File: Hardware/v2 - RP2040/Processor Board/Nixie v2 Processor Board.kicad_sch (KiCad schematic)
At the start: 82 parts, among them J1 Conn_01x10_Socket, J2 USB_C_Receptacle_USB2.0, J3 Conn_01x03_2.54mm, J4 Conn_01x03_2.54mm, J5 AudioJack3_SwitchT, J6 Conn_01x10_Socket, J8 Conn_01x01_Pin, J9 Conn_01x10_Socket, Q1 PZTA92, Q3 MMBTA42, SW1 SW_Push, SW2 SW_Push, SW3 SW_DIP_x10, SW4 SW_Push, U1 NCH8200HV, U10 W25Q128JVP, U12 DS3231MZ, U14 VEML7700, U3 TPS62933, U7 MCP23017_ML, U8 AP22913, U9 RP2040, Y1 12MHz

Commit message: seperated the processor and nixie boards
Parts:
- removed C2: 4.7u, Capacitor_THT:CP_Radial_D8.0mm_P3.50mm, symbol Device:C_Polarized_Small_US
- removed C3, C31, C5: 100n, Capacitor_SMD:C_0603_1608Metric, symbol Device:C_Small
- removed C30: 10u, symbol Device:C_Polarized_Small_US
- removed C4: 10u, Capacitor_SMD:C_0603_1608Metric, symbol Device:C_Small
- removed C6: 82p, Capacitor_SMD:C_0603_1608Metric, symbol Device:C_Small
- removed C7: 33n, Capacitor_SMD:C_0603_1608Metric, symbol Device:C_Small
- removed C8: 47u, Capacitor_SMD:C_0603_1608Metric, symbol Device:C_Small
- removed L1: 7.8u, Inductor_SMD:L_Vishay_IHLP-5050, symbol Device:L
- removed Q1: PZTA92, Package_TO_SOT_SMD:SOT-223-3_TabPin2, symbol Transistor_BJT:PZTA92
- removed Q3: MMBTA42, Package_TO_SOT_SMD:SOT-23, symbol Transistor_BJT:MMBTA42
- removed R17: 30.9, Resistor_SMD:R_0603_1608Metric, symbol Device:R_Small_US
- removed R18, R7: 10k, Resistor_SMD:R_0603_1608Metric, symbol Device:R_Small_US
- removed R28, R29: 2.2k, Resistor_SMD:R_0603_1608Metric, symbol Device:R_Small_US
- removed R5: 100k, Resistor_SMD:R_0603_1608Metric, symbol Device:R_Small_US
- removed TP3: TestPoint, symbol Connector:TestPoint
- removed U1: NCH8200HV, symbol Nick-Nixie:NCH8200HV
- removed U14: VEML7700, symbol Nick_Sensor:VEML7700
- removed U3: TPS62933, Package_TO_SOT_SMD:SOT-583-8, symbol Regulator_Switching:TPS62933
- added C19: 1u, Capacitor_SMD:C_0402_1005Metric, symbol Device:C_Small
- added C2: 22u, Capacitor_SMD:C_0603_1608Metric, symbol Device:C_Small
- added JP1: SolderJumper_3_Open, Jumper:SolderJumper-3_P1.3mm_Open_RoundedPad1.0x1.5mm, symbol Jumper:SolderJumper_3_Open
- added R10: 2.2k, Resistor_SMD:R_0603_1608Metric, symbol Device:R_Small_US
- added R13: 10k, Resistor_SMD:R_0603_1608Metric, symbol Device:R_Small_US
- added TP10, TP6, TP7, TP8, TP9: TestPoint, TestPoint:TestPoint_Pad_D2.0mm, symbol Connector:TestPoint
- added U1: TPS82084SIL, symbol Nick_Converter:TPS82084SIL
- C1: value 100u -> 10u
- C10: renamed from C14; footprint Capacitor_SMD:C_0603_1608Metric -> Capacitor_SMD:C_0402_1005Metric
- C11: renamed from C15; footprint Capacitor_SMD:C_0603_1608Metric -> Capacitor_SMD:C_0402_1005Metric
- C12: renamed from C16; footprint Capacitor_SMD:C_0603_1608Metric -> Capacitor_SMD:C_0402_1005Metric
- C13: renamed from C17; footprint Capacitor_SMD:C_0603_1608Metric -> Capacitor_SMD:C_0402_1005Metric
- C5: renamed from C9; footprint Capacitor_SMD:C_0603_1608Metric -> Capacitor_SMD:C_0402_1005Metric
- C6: renamed from C10; footprint Capacitor_SMD:C_0603_1608Metric -> Capacitor_SMD:C_0402_1005Metric
- C7: renamed from C11; footprint Capacitor_SMD:C_0603_1608Metric -> Capacitor_SMD:C_0402_1005Metric
- C8: renamed from C12; footprint Capacitor_SMD:C_0603_1608Metric -> Capacitor_SMD:C_0402_1005Metric
- C9: renamed from C13; footprint Capacitor_SMD:C_0603_1608Metric -> Capacitor_SMD:C_0402_1005Metric
- J1: renamed from J9; footprint (none) -> Connector_PinSocket_2.54mm:PinSocket_2x05_P2.54mm_Horizontal
- J2: renamed from J1; footprint (none) -> Connector_PinSocket_2.54mm:PinSocket_2x05_P2.54mm_Horizontal
- J3: renamed from J6; footprint (none) -> Connector_PinSocket_2.54mm:PinSocket_2x05_P2.54mm_Horizontal
- J4: renamed from J8; footprint (none) -> Connector_PinHeader_2.54mm:PinHeader_1x01_P2.54mm_Vertical
- R1: value 100k -> 523k
- R2: value 10k -> 169k; footprint Resistor_SMD:R_0402_1005Metric -> Resistor_SMD:R_0603_1608Metric
- R3: value 100k -> 499k
- R9: value 10k -> 2.2k
- TP1, TP2: footprint (none) -> TestPoint:TestPoint_Pad_D2.0mm
- TP3: renamed from TP6; footprint (none) -> TestPoint:TestPoint_Pad_D2.0mm
- TP4: renamed from TP5; footprint (none) -> TestPoint:TestPoint_Pad_D2.0mm
- TP5: renamed from TP4; footprint (none) -> TestPoint:TestPoint_Pad_D2.0mm
- Y1: footprint 0_My_Footprints:Crystal_SMD_Abracon_ABM10-4Pin_2.5x2.0mm -> Crystal:Crystal_SMD_Abracon_ABM10-4Pin_2.5x2.0mm
- renumbered C18 to C14, C19 to C15, C20 to C16, C29 to C17, C21 to C18, C27 to C20, C28 to C21, C33 to C22, C35 to C23, C22 to C3, C23 to C4, J2 to J6, J3 to J7, J4 to J8, R24 to R11, R25 to R12, R27 to R14, R32 to R15, R30 to R16, R31 to R17, R19 to R4, R20 to R5, R21 to R6, R22 to R7, R23 to R8, U8 to U2, U12 to U3, U9 to U4, U10 to U5, U7 to U6
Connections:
- net Mins_Ones_A is gone; now on net Minutes_Ones_A: J2.9 (Pin_9)
- net Mins_Ones_B is gone; now on net Minutes_Ones_B: J2.7 (Pin_7)
- net Mins_Ones_C is gone; now on net Minutes_Ones_C: J2.6 (Pin_6)
- net Mins_Ones_D is gone; now on net Minutes_Ones_D: J2.8 (Pin_8)
- net Mins_Tens_A is gone; now on net Minutes_Tens_A: J2.2 (Pin_2)
- net Mins_Tens_B is gone; now on net Minutes_Tens_B: J2.4 (Pin_4)
- net Mins_Tens_C is gone; now on net Minutes_Tens_C: J2.5 (Pin_5)
- net Mins_Tens_D is gone; now on net Minutes_Tens_D: J2.3 (Pin_3)
- net +3.3V: now also J3.3 (Pin_3), R1.2, R3.2, C2.1, JP1.3 (B), U1.5 (Vout); no longer R2.2
- net +3V3: now also R9.1, R10.1, R13.1
- net Dimming: now also J3.6 (Pin_6); no longer J3.5 (Pin_5)
- net GND: now also R2.1, C19.2, C2.2, U1.5 (Vout), U1.6 (GND), U1.EP (GND); no longer R9.2
- net Hours_Tens_A: now also U4.8 (GPIO6); no longer U4.4 (GPIO2)
- net Hours_Tens_B: now also U4.11 (GPIO8); no longer J3.4 (Pin_4), U3.8 (SCL), U4.7 (GPIO5), U6.8 (SCK)
- net Hours_Tens_C: now also U4.12 (GPIO9); no longer U4.8 (GPIO6)
- net Hours_Tens_D: now also U4.9 (GPIO7); no longer U4.5 (GPIO3)
- net RTC_Interrupt: now also U4.37 (GPIO25), R13.2; no longer U4.36 (GPIO24)
- net Settings_Interrupt: now also U4.38 (GPIO26_ADC0); no longer U4.37 (GPIO25)
- net UART1_RX: now also U4.7 (GPIO5); no longer U4.12 (GPIO9)
- net UART1_TX: now also U4.6 (GPIO4); no longer U4.11 (GPIO8)
- net VBUS: now also JP1.1 (A), U1.1 (EN), U1.3 (Vin), U1.4 (Vin); no longer C3.1, U2.4 (VIN), U2.6 (VIN)
- net at U6.20 (GPA3): now also TP6.1
- net at U6.21 (GPA4): now also TP7.1
- net at U6.22 (GPA5): now also TP8.1
- net at U6.23 (GPA6): now also TP9.1
- net at U6.24 (GPA7): now also TP10.1
- net at R3.1: now also U1.2 (PG); no longer R1.2
- net at BT1.1 (+), U3.6 (VBAT): now also C19.1
- net 170V_1: no longer names the net of R1.1
- net 170V_1: now also R2.2, U1.7 (FB)
- net GPS_Presence renamed GPS_Connected
- net GPS_Connected: now also U4.36 (GPIO24); no longer U4.38 (GPIO26_ADC0)
- net I2C0_SDA renamed I2C1_SDA
- net I2C1_SDA: now also J3.4 (Pin_4), U4.4 (GPIO2), R10.2; no longer J3.3 (Pin_3), U4.6 (GPIO4)
- new net: C3.1, JP1.2 (C), U2.4 (VIN), U2.6 (VIN)
- new net I2C1_SCL: J3.5 (Pin_5), R9.2, U3.8 (SCL), U4.5 (GPIO3), U6.8 (SCK)
- no-connect marks 8 -> 3
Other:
- note added: "3mOhm"
- note added: "9mOhm"
- note added: "VBUS to 3.3V"
- note added: "Voltage select for GPS module"
- note removed: "250V or larger"
- note removed: "LIGHT SENSOR"
- note removed: "Low ESR"
- note removed: "Vin to 3.3V"
- title: Nixie Tube Clock -> Nixie Processor Board
- moved on the sheet: BT1, C10, C11, C12, C13, C14, C15, C16, C17, C18, C20, C21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

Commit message: Started board layout
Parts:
- added H1, H2, H3, H4: MountingHole_Pad, MountingHole:MountingHole_3.2mm_M3_Pad_Via, symbol Mechanical:MountingHole_Pad
- C19: footprint Capacitor_SMD:C_0402_1005Metric -> Capacitor_SMD:C_0603_1608Metric
- J5: footprint (none) -> Connector_Audio:Jack_3.5mm_CUI_SJ-3524-SMT_Horizontal
- JP1: footprint Jumper:SolderJumper-3_P1.3mm_Open_RoundedPad1.0x1.5mm -> Jumper:SolderJumper-3_P1.3mm_Open_RoundedPad1.0x1.5mm_NumberLabels
- SW3: footprint Button_Switch_SMD:SW_DIP_SPSTx10_Slide_6.7x26.96mm_W6.73mm_P2.54mm_LowProfile_JPin -> Button_Switch_THT:SW_DIP_SPSTx10_Piano_10.8x26.96mm_W7.62mm_P2.54mm
- U1: footprint (none) -> Nick_Converter_DCDC:MicroSiP 1.33mm
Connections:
- net +3.3V: now also U1.8 (Vout); no longer U1.5 (Vout)
- net GND: now also J1.5 (Pin_5), J1.6 (Pin_6), J2.5 (Pin_5), J2.6 (Pin_6), SW3.1, SW3.10, SW3.2, SW3.3, SW3.4, SW3.5, SW3.6, SW3.7, SW3.8, SW3.9, U1.9 (GND), H1.1, H2.1, H3.1, H4.1; no longer J1.1 (Pin_1), J1.10 (Pin_10), J2.1 (Pin_1), J2.10 (Pin_10), SW3.11, SW3.12, SW3.13, SW3.14, SW3.15, SW3.16, SW3.17, SW3.18, SW3.19, SW3.20, U1.EP (GND)
- net Hours_Ones_A: now also J1.3 (Pin_3), U4.11 (GPIO8); no longer J1.9 (Pin_9), U4.13 (GPIO10)
- net Hours_Ones_B: now also J1.1 (Pin_1), U4.8 (GPIO6); no longer J1.7 (Pin_7), U4.15 (GPIO12)
- net Hours_Ones_C: now also J1.2 (Pin_2), U4.9 (GPIO7); no longer J1.6 (Pin_6), U4.16 (GPIO13)
- net Hours_Ones_D: now also J1.4 (Pin_4), U4.12 (GPIO9); no longer J1.8 (Pin_8), U4.14 (GPIO11)
- net Hours_Tens_A: now also J1.10 (Pin_10), U4.16 (GPIO13); no longer J1.2 (Pin_2), U4.8 (GPIO6)
- net Hours_Tens_B: now also J1.8 (Pin_8), U4.14 (GPIO11); no longer J1.4 (Pin_4), U4.11 (GPIO8)
- net Hours_Tens_C: now also J1.7 (Pin_7), U4.13 (GPIO10); no longer J1.5 (Pin_5), U4.12 (GPIO9)
- net Hours_Tens_D: now also J1.9 (Pin_9), U4.15 (GPIO12); no longer J1.3 (Pin_3), U4.9 (GPIO7)
- net Minutes_Ones_A: now also J2.3 (Pin_3), U4.27 (GPIO16); no longer J2.9 (Pin_9), U4.29 (GPIO18)
- net Minutes_Ones_B: now also J2.1 (Pin_1), U4.18 (GPIO15); no longer J2.7 (Pin_7), U4.31 (GPIO20)
- net Minutes_Ones_C: now also J2.2 (Pin_2), U4.17 (GPIO14); no longer J2.6 (Pin_6), U4.32 (GPIO21)
- net Minutes_Ones_D: now also J2.4 (Pin_4), U4.28 (GPIO17); no longer J2.8 (Pin_8), U4.30 (GPIO19)
- net Minutes_Tens_A: now also J2.10 (Pin_10), U4.32 (GPIO21); no longer J2.2 (Pin_2), U4.17 (GPIO14)
- net Minutes_Tens_B: now also J2.8 (Pin_8), U4.29 (GPIO18); no longer J2.4 (Pin_4), U4.27 (GPIO16)
- net Minutes_Tens_C: now also J2.7 (Pin_7), U4.30 (GPIO19); no longer J2.5 (Pin_5), U4.28 (GPIO17)
- net Minutes_Tens_D: now also J2.9 (Pin_9), U4.31 (GPIO20); no longer J2.3 (Pin_3), U4.18 (GPIO15)
- net at C23.1, SW4.1: now also U6.27 (GPB2); no longer U6.19 (GPA2)
- net at U6.1 (GPB4): now also TP7.1; no longer SW3.5
- net at U6.17 (GPA0): now also SW3.20; no longer SW3.9
- net at U6.18 (GPA1): now also SW3.19; no longer SW3.10
- net at U6.2 (GPB5): now also TP8.1; no longer SW3.6
- net at U6.20 (GPA3): now also SW3.17; no longer TP6.1
- net at U6.21 (GPA4): now also SW3.16; no longer TP7.1
- net at U6.22 (GPA5): now also SW3.15; no longer TP8.1
- net at U6.23 (GPA6): now also SW3.14; no longer TP9.1
- net at U6.24 (GPA7): now also SW3.13; no longer TP10.1
- net at U6.25 (GPB0): now also SW3.12; no longer SW3.1
- net at U6.26 (GPB1): now also SW3.11; no longer SW3.2
- net at U6.28 (GPB3): now also TP6.1; no longer SW3.4
- net at U6.3 (GPB6): now also TP9.1; no longer SW3.7
- net at U6.4 (GPB7): now also TP10.1; no longer SW3.8
- new net: SW3.18, U6.19 (GPA2)
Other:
- moved on the sheet: C23, J3, SW4

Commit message: Laied out indivdual circuit blocks
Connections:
- net +3.3V is gone; now on net +3V3: C10.1, C11.1, C12.1, C13.1, C15.1, C2.1, C7.1, C8.1, C9.1, J3.3 (Pin_3), JP1.3 (B), R1.2, R11.2, R3.2, R8.2, U1.8 (Vout), U4.1 (IOVDD), U4.10 (IOVDD), U4.22 (IOVDD), U4.33 (IOVDD), U4.42 (IOVDD), U4.43 (ADC_AVDD), U4.44 (VREG_IN), U4.48 (USB_VDD), U4.49 (IOVDD)
- net USB_RP_D+: now reaches R5.1, U4.47 (USB_DP)
- net USB_D+: now reaches J6.A6 (D+), J6.B6 (D+), R5.2
- net USB_D-: now reaches J6.A7 (D-), J6.B7 (D-), R4.2
- net USB_RP_D-: now reaches R4.1, U4.46 (USB_DM)
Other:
- moved on the sheet: R4, R5

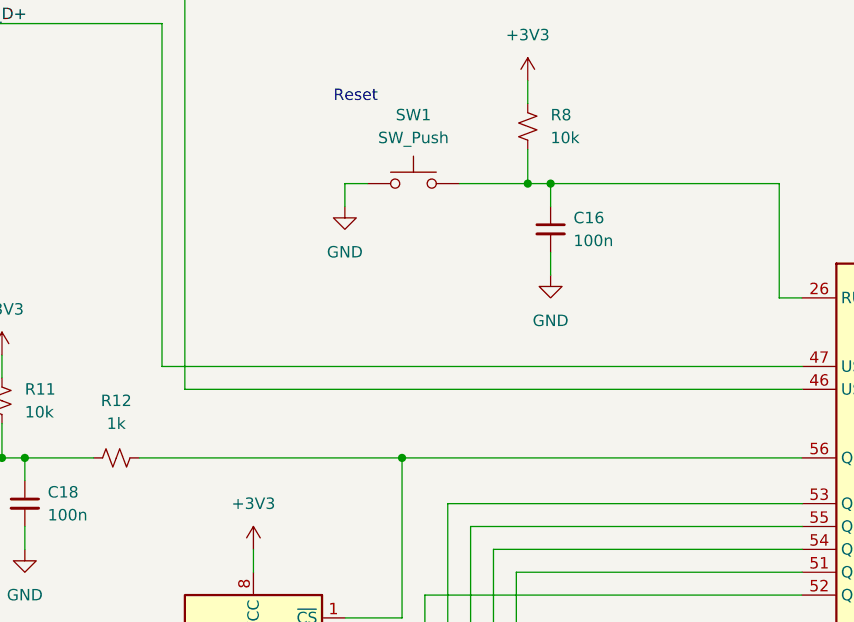
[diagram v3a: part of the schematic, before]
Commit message: Started placing assembled blocks on the board and routing
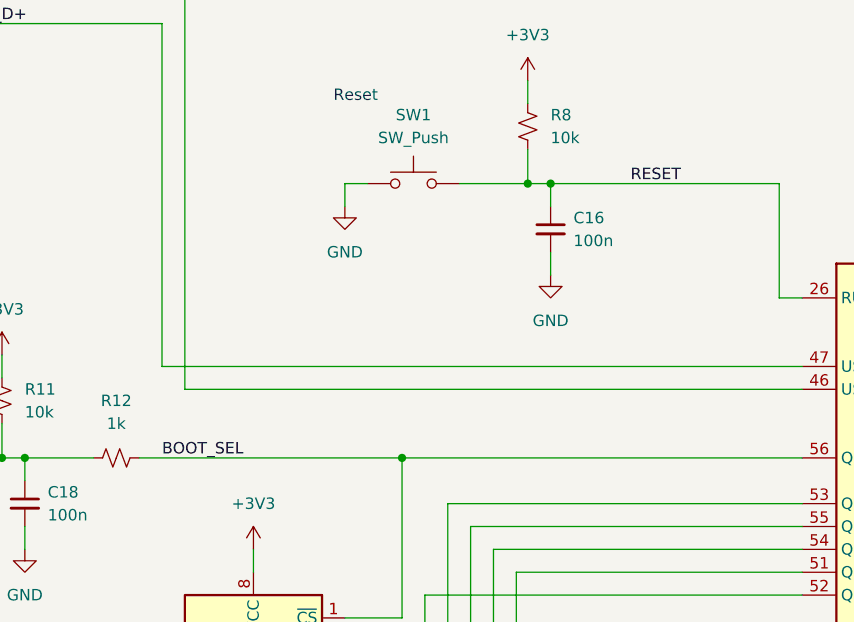
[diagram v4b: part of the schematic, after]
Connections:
- net BOOT_SEL: now reaches R12.1, U4.56 (QSPI_SS), U5.1 (~{CS})
- net RESET: now reaches C16.1, R8.1, SW1.2, U4.26 (RUN)
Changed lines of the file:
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@@
+		)
+	)
+	(label "BOOT_SEL"
+		(at 120.65 207.01 0)
+		(fields_autoplaced yes)
+		(effects
+			(font
+				(size 1.27 1.27)
+			)
+			(justify left bottom)
 		)
 	)
@@
 		(fields_autoplaced yes)
 		(effects
+			(font
+				(size 1.27 1.27)
+			)
+			(justify left bottom)
+		)
+	)
+	(label "RESET"
+		(at 172.72 176.53 0)
+		(fields_autoplaced yes)
+		(effects

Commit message: started nixie layout, added bleed resistor to HV cap
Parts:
- J1, J2, J3: footprint Connector_PinSocket_2.54mm:PinSocket_2x05_P2.54mm_Horizontal -> Connector_PinSocket_2.54mm:PinSocket_2x05_P2.54mm_Vertical
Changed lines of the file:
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@@
 			)
 		)
-		(property "Footprint" "Connector_PinSocket_2.54mm:PinSocket_2x05_P2.54mm_Horizontal"
+		(property "Footprint" "Connector_PinSocket_2.54mm:PinSocket_2x05_P2.54mm_Vertical"
 			(at 447.04 44.45 0)
 			(effects
@@
 			)
 		)
-		(property "Footprint" "Connector_PinSocket_2.54mm:PinSocket_2x05_P2.54mm_Horizontal"
+		(property "Footprint" "Connector_PinSocket_2.54mm:PinSocket_2x05_P2.54mm_Vertical"
 			(at 497.84 44.45 0)
 			(effects
@@
 			)
 		)
-		(property "Footprint" "Connector_PinSocket_2.54mm:PinSocket_2x05_P2.54mm_Horizontal"
+		(property "Footprint" "Connector_PinSocket_2.54mm:PinSocket_2x05_P2.54mm_Vertical"
 			(at 396.24 44.45 0)
 			(effects

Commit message: finished initial layout and swapped SDA/SCL on connector
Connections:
- net I2C1_SCL: now also J3.4 (Pin_4); no longer J3.5 (Pin_5)
- net I2C1_SDA: now also J3.5 (Pin_5); no longer J3.4 (Pin_4)
- net BOOT_SEL: no longer names the net of R12.1, U4.56 (QSPI_SS), U5.1 (~{CS})
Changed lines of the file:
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@@
 	(wire
 		(pts
-			(xy 353.06 82.55) (xy 497.84 82.55)
-		)
-		(stroke
-			(width 0)
-			(type default)
-		)
-	)
-	(wire
-		(pts
 			(xy 426.72 203.2) (xy 407.67 203.2)
 		)
@@
 		)
 	)
+	(wire
+		(pts
+			(xy 497.84 49.53) (xy 497.84 85.09)
+		)
+		(stroke
+			(width 0)
+			(type default)
+		)
+	)
 	(bus
 		(pts
@@
 	(wire
 		(pts
+			(xy 495.3 49.53) (xy 495.3 82.55)
+		)
+		(stroke
+			(width 0)
+			(type default)
+		)
+	)
+	(wire
+		(pts
 			(xy 185.42 257.81) (xy 185.42 298.45)
 		)
@@
 	(wire
 		(pts
-			(xy 497.84 49.53) (xy 497.84 82.55)
-		)
-		(stroke
-			(width 0)
-			(type default)
-		)
-	)
-	(wire
-		(pts
 			(xy 382.27 232.41) (xy 379.73 232.41)
 		)
@@
 	(wire
 		(pts
-			(xy 495.3 49.53) (xy 495.3 85.09)
-		)
-		(stroke
-			(width 0)
-			(type default)
-		)
-	)
-	(wire
-		(pts
 			(xy 439.42 331.47) (xy 439.42 334.01)
 		)
@@
 	(wire
 		(pts
+			(xy 353.06 82.55) (xy 495.3 82.55)
+		)
+		(stroke
+			(width 0)
+			(type default)
+		)
+	)
+	(wire
+		(pts
 			(xy 467.36 339.09) (xy 467.36 341.63)
 		)
@@
 	(wire
 		(pts
-			(xy 355.6 85.09) (xy 495.3 85.09)
+			(xy 355.6 85.09) (xy 497.84 85.09)
 		)
 		(stroke
@@
 		)
 	)
-	(label "I2C1_SCL"
-		(at 497.84 73.66 90)
-		(fields_autoplaced yes)
-		(effects
-			(font
-				(size 1.27 1.27)
-			)
-			(justify left bottom)
-		)
-	)
 	(label "USB_RP_D+"
 		(at 95.25 158.75 0)
@@
 		)
 	)
+	(label "I2C1_SCL"
+		(at 495.3 73.66 90)
+		(fields_autoplaced yes)
+		(effects
+			(font
+				(size 1.27 1.27)
+			)
+			(justify left bottom)
+		)
+	)
 	(label "Settings_Interrupt"
 		(at 361.95 308.61 0)
@@
 	)
 	(label "I2C1_SDA"
-		(at 361.95 213.36 0)
+		(at 497.84 73.66 90)
 		(fields_autoplaced yes)
 		(effects
@@
 		)
 	)
-	(label "BOOT_SEL"
-		(at 120.65 207.01 0)
+	(label "I2C1_SDA"
+		(at 361.95 213.36 0)
 		(fields_autoplaced yes)
 		(effects
@@
 		(fields_autoplaced yes)
 		(effects
-			(font
-				(size 1.27 1.27)
-			)
-			(justify left bottom)
-		)
-	)
-	(label "I2C1_SDA"
-		(at 495.3 73.66 90)
-		(fields_autoplaced yes)
-		(effects
